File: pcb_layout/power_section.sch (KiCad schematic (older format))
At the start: 23 parts, among them Q1 NXP BSS84, U2 MCP73831/2, U3 TPS736

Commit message: More modules, initial pcb layout
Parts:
- C4: footprint Capacitors_SMD:C_0805 -> Capacitors_SMD:C_1206
- C5: value 4.7u -> 4.7uF; footprint Capacitors_SMD:C_0805 -> Capacitors_SMD:C_1206
- RF_Current1: footprint Socket_Strips:Socket_Strip_Angled_1x02_Pitch2.54mm -> Socket_Strips:Socket_Strip_Straight_1x02_Pitch2.54mm
- renumbered BATTERY1 to Battery_Input1, D2 to D1, D1 to Power_LED1
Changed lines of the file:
@@
 $EndDescr
 $Comp
-L GND #PWR19
+L GND #PWR09
 U 1 1 589A2DFC
 P 7850 2650
-F 0 "#PWR19" H 7850 2400 50  0001 C CNN
+F 0 "#PWR09" H 7850 2400 50  0001 C CNN
 F 1 "GND" H 7850 2500 50  0000 C CNN
 F 2 "" H 7850 2650 50  0000 C CNN
@@
 $EndComp
 $Comp
-L +3.3V #PWR16
+L +3.3V #PWR010
 U 1 1 589A2E1E
 P 6550 4050
-F 0 "#PWR16" H 6550 3900 50  0001 C CNN
+F 0 "#PWR010" H 6550 3900 50  0001 C CNN
 F 1 "+3.3V" H 6550 4190 50  0000 C CNN
 F 2 "" H 6550 4050 50  0000 C CNN
@@
 U 1 1 589A2E2B
 P 7200 3800
-F 0 "MCU_Current1" H 7200 3950 50  0000 C CNN
+F 0 "MCU_Current1" V 7400 3800 50  0000 C CNN
 F 1 "CONN_01X02" V 7300 3800 50  0000 C CNN
 F 2 "Socket_Strips:Socket_Strip_Straight_1x02_Pitch2.54mm" H 7200 3800 50  0001 C CNN
@@
 U 1 1 589A2E32
 P 7200 4650
-F 0 "RF_Current1" H 7200 4800 50  0000 C CNN
+F 0 "RF_Current1" V 7400 4650 50  0000 C CNN
 F 1 "CONN_01X02" V 7300 4650 50  0000 C CNN
-F 2 "Socket_Strips:Socket_Strip_Angled_1x02_Pitch2.54mm" H 7200 4650 50  0001 C CNN
+F 2 "Socket_Strips:Socket_Strip_Straight_1x02_Pitch2.54mm" H 7200 4650 50  0001 C CNN
 F 3 "" H 7200 4650 50  0000 C CNN
 	1    7200 4650
@@
 RF_POW
 $Comp
-L CONN_01X02 BATTERY1
+L CONN_01X02 Battery_Input1
 U 1 1 589A2E3B
 P 2700 2000
-F 0 "BATTERY1" H 2700 2300 50  0000 C CNN
+F 0 "Battery_Input1" H 2700 2300 50  0000 C CNN
 F 1 "CONN_01X02" V 2800 2000 50  0000 C CNN
 F 2 "Socket_Strips:Socket_Strip_Straight_1x02_Pitch2.54mm" H 2700 2000 50  0001 C CNN
@@
 $EndComp
 $Comp
-L GND #PWR10
+L GND #PWR011
 U 1 1 589A2E42
 P 2900 2700
-F 0 "#PWR10" H 2900 2450 50  0001 C CNN
+F 0 "#PWR011" H 2900 2450 50  0001 C CNN
 F 1 "GND" H 2900 2550 50  0000 C CNN
 F 2 "" H 2900 2700 50  0000 C CNN
@@
 $EndComp
 $Comp
-L GND #PWR12
+L GND #PWR012
 U 1 1 589A2E4F
 P 4000 2700
-F 0 "#PWR12" H 4000 2450 50  0001 C CNN
+F 0 "#PWR012" H 4000 2450 50  0001 C CNN
 F 1 "GND" H 4000 2550 50  0000 C CNN
 F 2 "" H 4000 2700 50  0000 C CNN
@@
 $EndComp
 $Comp
-L D_Zener D2
+L D_Zener D1
 U 1 1 589A2E55
 P 4400 2150
-F 0 "D2" H 4400 2250 50  0000 C CNN
+F 0 "D1" H 4400 2250 50  0000 C CNN
 F 1 "D_Zener" H 4400 2050 50  0000 C CNN
 F 2 "Diodes_SMD:D_SMA_Handsoldering" H 4400 2150 50  0001 C CNN
@@
 $EndComp
 $Comp
-L GND #PWR9
+L GND #PWR013
 U 1 1 589A2E64
 P 2450 4150
-F 0 "#PWR9" H 2450 3900 50  0001 C CNN
+F 0 "#PWR013" H 2450 3900 50  0001 C CNN
 F 1 "GND" H 2450 4000 50  0000 C CNN
 F 2 "" H 2450 4150 50  0000 C CNN
@@
 VUSB
 $Comp
-L LED D1
+L LED Power_LED1
 U 1 1 589A2E6D
 P 3550 3450
-F 0 "D1" H 3550 3550 50  0000 C CNN
+F 0 "Power_LED1" H 3550 3550 50  0000 C CNN
 F 1 "LED" H 3550 3350 50  0000 C CNN
 F 2 "LEDs:LED_0805" H 3550 3450 50  0001 C CNN
@@
 $EndComp
 $Comp
-L GND #PWR14
+L GND #PWR014
 U 1 1 589A2E83
 P 5050 4350
-F 0 "#PWR14" H 5050 4100 50  0001 C CNN
+F 0 "#PWR014" H 5050 4100 50  0001 C CNN
 F 1 "GND" H 5050 4200 50  0000 C CNN
 F 2 "" H 5050 4350 50  0000 C CNN
@@
 V_Battery
 $Comp
-L +3.3V #PWR17
+L +3.3V #PWR015
 U 1 1 589A2E91
 P 7400 2050
-F 0 "#PWR17" H 7400 1900 50  0001 C CNN
+F 0 "#PWR015" H 7400 1900 50  0001 C CNN
 F 1 "+3.3V" H 7400 2190 50  0000 C CNN
 F 2 "" H 7400 2050 50  0000 C CNN
@@
 $EndComp
 $Comp
-L GND #PWR15
+L GND #PWR016
 U 1 1 589A2E97
 P 5800 2350
-F 0 "#PWR15" H 5800 2100 50  0001 C CNN
+F 0 "#PWR016" H 5800 2100 50  0001 C CNN
 F 1 "GND" H 5800 2200 50  0000 C CNN
 F 2 "" H 5800 2350 50  0000 C CNN
@@
 $EndComp
 $Comp
-L GND #PWR18
+L GND #PWR017
 U 1 1 589A2EA4
 P 7400 2800
-F 0 "#PWR18" H 7400 2550 50  0001 C CNN
+F 0 "#PWR017" H 7400 2550 50  0001 C CNN
 F 1 "GND" H 7400 2650 50  0000 C CNN
 F 2 "" H 7400 2800 50  0000 C CNN
@@
 F 0 "C4" H 3475 2450 50  0000 L CNN
 F 1 "4.7uF" H 3475 2250 50  0000 L CNN
-F 2 "Capacitors_SMD:C_0805" H 3488 2200 50  0001 C CNN
+F 2 "Capacitors_SMD:C_1206" H 3488 2200 50  0001 C CNN
 F 3 "" H 3450 2350 50  0000 C CNN
 	1    3450 2350
@@
 $EndComp
 $Comp
-L GND #PWR11
+L GND #PWR018
 U 1 1 589A2EB1
 P 3450 2700
-F 0 "#PWR11" H 3450 2450 50  0001 C CNN
+F 0 "#PWR018" H 3450 2450 50  0001 C CNN
 F 1 "GND" H 3450 2550 50  0000 C CNN
 F 2 "" H 3450 2700 50  0000 C CNN
@@
 U 1 1 589A2EBE
 P 3550 4500
-F 0 "Charge_Current1" H 3550 4650 50  0000 C CNN
+F 0 "Charge_Current1" V 3750 4500 50  0000 C CNN
 F 1 "CONN_01X02" V 3650 4500 50  0000 C CNN
 F 2 "Socket_Strips:Socket_Strip_Straight_2x01_Pitch2.54mm" H 3550 4500 50  0001 C CNN
@@
 P 4750 4350
 F 0 "C5" H 4775 4450 50  0000 L CNN
-F 1 "4.7u" H 4775 4250 50  0000 L CNN
-F 2 "Capacitors_SMD:C_0805" H 4788 4200 50  0001 C CNN
+F 1 "4.7uF" H 4775 4250 50  0000 L CNN
+F 2 "Capacitors_SMD:C_1206" H 4788 4200 50  0001 C CNN
 F 3 "" H 4750 4350 50  0000 C CNN
 	1    4750 4350
@@
 $EndComp
 $Comp
-L GND #PWR13
+L GND #PWR019
 U 1 1 589A2ED3
 P 4750 4550
-F 0 "#PWR13" H 4750 4300 50  0001 C CNN
+F 0 "#PWR019" H 4750 4300 50  0001 C CNN
 F 1 "GND" H 4750 4400 50  0000 C CNN
 F 2 "" H 4750 4550 50  0000 C CNN
@@
 	8950 3100 9450 3100
 $Comp
-L GND #PWR20
+L GND #PWR020
 U 1 1 589A521E
 P 9050 3700
-F 0 "#PWR20" H 9050 3450 50  0001 C CNN
+F 0 "#PWR020" H 9050 3450 50  0001 C CNN
 F 1 "GND" H 9050 3550 50  0000 C CNN
 F 2 "" H 9050 3700 50  0000 C CNN
@@
 3.3V
 $Comp
-L +3.3V #PWR21
+L +3.3V #PWR021
 U 1 1 589A66AD
 P 9550 3100
-F 0 "#PWR21" H 9550 2950 50  0001 C CNN
+F 0 "#PWR021" H 9550 2950 50  0001 C CNN
 F 1 "+3.3V" H 9550 3240 50  0000 C CNN
 F 2 "" H 9550 3100 50  0000 C CNN

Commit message: Added PCB LAyout
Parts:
- Battery_Current1, Charge_Current1: footprint Socket_Strips:Socket_Strip_Straight_2x01_Pitch2.54mm -> Pin_Headers:Pin_Header_Straight_1x02_Pitch2.54mm
- Battery_Input1: footprint Socket_Strips:Socket_Strip_Straight_1x02_Pitch2.54mm -> Pin_Headers:Pin_Header_Angled_1x02_Pitch2.54mm
- MCU_Current1, RF_Current1: footprint Socket_Strips:Socket_Strip_Straight_1x02_Pitch2.54mm -> Pin_Headers:Pin_Header_Straight_1x02_Pitch2.54mm
- Power_LED1: symbol LED -> LED-RESCUE-lora_sensor
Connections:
- net labels removed: Gnd
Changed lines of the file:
@@
 LIBS:mcp9700t-e
 LIBS:rn2483
+LIBS:fa_238
 LIBS:lora_sensor-cache
-EELAYER 25 0
+EELAYER 26 0
 EELAYER END
 $Descr A4 11693 8268
@@
 F 0 "MCU_Current1" V 7400 3800 50  0000 C CNN
 F 1 "CONN_01X02" V 7300 3800 50  0000 C CNN
-F 2 "Socket_Strips:Socket_Strip_Straight_1x02_Pitch2.54mm" H 7200 3800 50  0001 C CNN
+F 2 "Pin_Headers:Pin_Header_Straight_1x02_Pitch2.54mm" H 7200 3800 50  0001 C CNN
 F 3 "" H 7200 3800 50  0000 C CNN
 	1    7200 3800
@@
 F 0 "RF_Current1" V 7400 4650 50  0000 C CNN
 F 1 "CONN_01X02" V 7300 4650 50  0000 C CNN
-F 2 "Socket_Strips:Socket_Strip_Straight_1x02_Pitch2.54mm" H 7200 4650 50  0001 C CNN
+F 2 "Pin_Headers:Pin_Header_Straight_1x02_Pitch2.54mm" H 7200 4650 50  0001 C CNN
 F 3 "" H 7200 4650 50  0000 C CNN
 	1    7200 4650
@@
 F 0 "Battery_Input1" H 2700 2300 50  0000 C CNN
 F 1 "CONN_01X02" V 2800 2000 50  0000 C CNN
-F 2 "Socket_Strips:Socket_Strip_Straight_1x02_Pitch2.54mm" H 2700 2000 50  0001 C CNN
+F 2 "Pin_Headers:Pin_Header_Angled_1x02_Pitch2.54mm" H 2700 2000 50  0001 C CNN
 F 3 "" H 2700 2000 50  0000 C CNN
 	1    2700 2000
@@
 VUSB
 $Comp
-L LED Power_LED1
+L LED-RESCUE-lora_sensor Power_LED1
 U 1 1 589A2E6D
 P 3550 3450
+AR Path="/589A2E6D" Ref="Power_LED1"  Part="1"
+AR Path="/5899E1BE/589A2E6D" Ref="Power_LED1"  Part="1"
 F 0 "Power_LED1" H 3550 3550 50  0000 C CNN
 F 1 "LED" H 3550 3350 50  0000 C CNN
@@
 F 0 "Battery_Current1" V 6300 1850 50  0000 C CNN
 F 1 "CONN_01X02" V 6250 1850 50  0000 C CNN
-F 2 "Socket_Strips:Socket_Strip_Straight_2x01_Pitch2.54mm" H 6150 1850 50  0001 C CNN
+F 2 "Pin_Headers:Pin_Header_Straight_1x02_Pitch2.54mm" H 6150 1850 50  0001 C CNN
 F 3 "" H 6150 1850 50  0000 C CNN
 	1    6150 1850
@@
 F 0 "Charge_Current1" V 3750 4500 50  0000 C CNN
 F 1 "CONN_01X02" V 3650 4500 50  0000 C CNN
-F 2 "Socket_Strips:Socket_Strip_Straight_2x01_Pitch2.54mm" H 3550 4500 50  0001 C CNN
+F 2 "Pin_Headers:Pin_Header_Straight_1x02_Pitch2.54mm" H 3550 4500 50  0001 C CNN
 F 3 "" H 3550 4500 50  0000 C CNN
 	1    3550 4500
@@
 	8950 3400 9450 3400
 Text HLabel 8950 3600 0    60   Input ~ 0
-Gnd
+GND
 Text HLabel 8950 3400 0    60   Input ~ 0
 RF_Power

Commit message: Finalized layout, added gerbers and renders
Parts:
- Battery_Input1: footprint Pin_Headers:Pin_Header_Angled_1x02_Pitch2.54mm -> Pin_Headers:Pin_Header_Straight_1x02_Pitch2.54mm
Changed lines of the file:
@@
 F 0 "Battery_Input1" H 2700 2300 50  0000 C CNN
 F 1 "CONN_01X02" V 2800 2000 50  0000 C CNN
-F 2 "Pin_Headers:Pin_Header_Angled_1x02_Pitch2.54mm" H 2700 2000 50  0001 C CNN
+F 2 "Pin_Headers:Pin_Header_Straight_1x02_Pitch2.54mm" H 2700 2000 50  0001 C CNN
 F 3 "" H 2700 2000 50  0000 C CNN
 	1    2700 2000

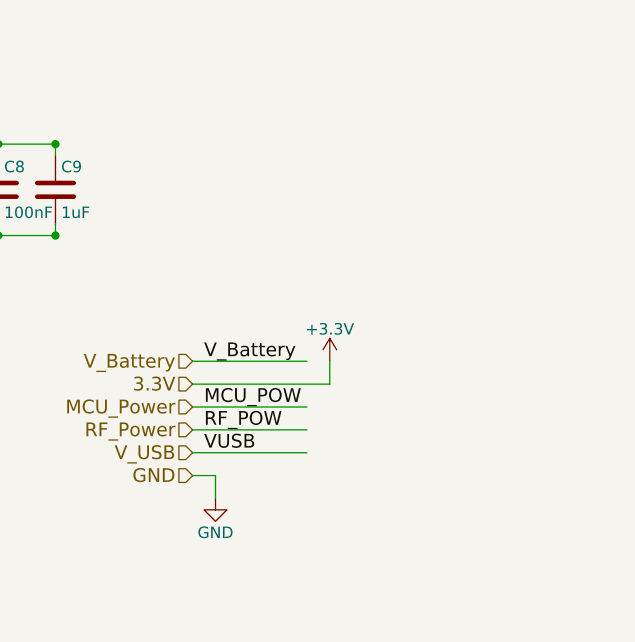
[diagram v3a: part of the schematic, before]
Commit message: More layout updates
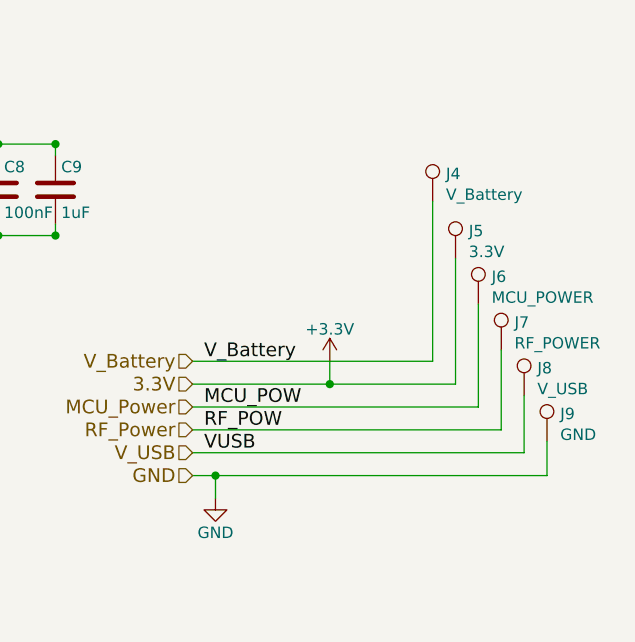
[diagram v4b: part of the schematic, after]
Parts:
- added J4: V_Battery, Measurement_Points:Measurement_Point_Square-SMD-Pad_Small, symbol TEST_1P
- added J5: 3.3V, Measurement_Points:Measurement_Point_Square-SMD-Pad_Small, symbol TEST_1P
- added J6: MCU_POWER, Measurement_Points:Measurement_Point_Square-SMD-Pad_Small, symbol TEST_1P
- added J7: RF_POWER, Measurement_Points:Measurement_Point_Square-SMD-Pad_Small, symbol TEST_1P
- added J8: V_USB, Measurement_Points:Measurement_Point_Square-SMD-Pad_Small, symbol TEST_1P
- added J9: GND, Measurement_Points:Measurement_Point_Square-TH_Big, symbol TEST_1P
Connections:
- wire segments 69 -> 75
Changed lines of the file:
@@
 V_Battery
 Wire Wire Line
-	8950 3100 9450 3100
+	8950 3100 10000 3100
 $Comp
 L GND #PWR020
@@
 V_Battery
 Wire Wire Line
-	8950 3600 9050 3600
+	8950 3600 10500 3600
 Wire Wire Line
 	9050 3600 9050 3700
 Wire Wire Line
-	8950 3200 9550 3200
+	8950 3200 10100 3200
 Text Label 9000 3300 0    60   ~ 0
 MCU_POW
@@
 RF_POW
 Wire Wire Line
-	8950 3300 9450 3300
+	8950 3300 10200 3300
 Wire Wire Line
-	8950 3400 9450 3400
+	8950 3400 10300 3400
 Text HLabel 8950 3600 0    60   Input ~ 0
 GND
@@
 VUSB
 Wire Wire Line
-	8950 3500 9450 3500
+	8950 3500 10400 3500
+$Comp
+L TEST_1P J4
+U 1 1 58A163E9
+P 10000 2400
+F 0 "J4" H 10058 2520 50  0000 L CNN
+F 1 "V_Battery" H 10058 2429 50  0000 L CNN
+F 2 "Measurement_Points:Measurement_Point_Square-SMD-Pad_Small" H 1850 950 50  0001 C CNN
+F 3 "" H 1850 950 50  0001 C CNN
+	1    10000 2400
+	1    0    0    -1
+$EndComp
+$Comp
+L TEST_1P J5
+U 1 1 58A16A2F
+P 10100 2650
+F 0 "J5" H 10158 2770 50  0000 L CNN
+F 1 "3.3V" H 10158 2679 50  0000 L CNN
+F 2 "Measurement_Points:Measurement_Point_Square-SMD-Pad_Small" H 1950 1200 50  0001 C CNN
+F 3 "" H 1950 1200 50  0001 C CNN
+	1    10100 2650
+	1    0    0    -1
+$EndComp
+$Comp
+L TEST_1P J6
+U 1 1 58A16A98
+P 10200 2850
+F 0 "J6" H 10258 2970 50  0000 L CNN
+F 1 "MCU_POWER" H 10258 2879 50  0000 L CNN
+F 2 "Measurement_Points:Measurement_Point_Square-SMD-Pad_Small" H 2050 1400 50  0001 C CNN
+F 3 "" H 2050 1400 50  0001 C CNN
+	1    10200 2850
+	1    0    0    -1
+$EndComp
+Wire Wire Line
+	10100 3200 10100 2650
+Connection ~ 9550 3200
+Wire Wire Line
+	10200 3300 10200 2850
+Wire Wire Line
+	10000 3100 10000 2400
+$Comp
+L TEST_1P J7
+U 1 1 58A16F1C
+P 10300 3050
+F 0 "J7" H 10358 3170 50  0000 L CNN
+F 1 "RF_POWER" H 10358 3079 50  0000 L CNN
+F 2 "Measurement_Points:Measurement_Point_Square-SMD-Pad_Small" H 2150 1600 50  0001 C CNN
+F 3 "" H 2150 1600 50  0001 C CNN
+	1    10300 3050
+	1    0    0    -1
+$EndComp
+Wire Wire Line
+	10300 3400 10300 3050
+$Comp
+L TEST_1P J8
+U 1 1 58A16FFC
+P 10400 3250
+F 0 "J8" H 10458 3370 50  0000 L CNN
+F 1 "V_USB" H 10458 3279 50  0000 L CNN
+F 2 "Measurement_Points:Measurement_Point_Square-SMD-Pad_Small" H 2250 1800 50  0001 C CNN
+F 3 "" H 2250 1800 50  0001 C CNN
+	1    10400 3250
+	1    0    0    -1
+$EndComp
+Wire Wire Line
+	10400 3500 10400 3250
+$Comp
+L TEST_1P J9
+U 1 1 58A170DB
+P 10500 3450
+F 0 "J9" H 10558 3570 50  0000 L CNN
+F 1 "GND" H 10558 3479 50  0000 L CNN
+F 2 "Measurement_Points:Measurement_Point_Square-TH_Big" H 2350 2000 50  0001 C CNN
+F 3 "" H 2350 2000 50  0001 C CNN
+	1    10500 3450
+	1    0    0    -1
+$EndComp
+Wire Wire Line
+	10500 3600 10500 3450
+Connection ~ 9050 3600
 $EndSCHEMATC

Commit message: Manufactured version
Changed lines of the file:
@@
 P 3550 3450
 AR Path="/589A2E6D" Ref="Power_LED1"  Part="1"
-AR Path="/5899E1BE/589A2E6D" Ref="Power_LED1"  Part="1"
-F 0 "Power_LED1" H 3550 3550 50  0000 C CNN
+AR Path="/5899E1BE/589A2E6D" Ref="Charge_LED1"  Part="1"
+F 0 "Charge_LED1" H 3550 3550 50  0000 C CNN
 F 1 "LED" H 3550 3350 50  0000 C CNN
 F 2 "LEDs:LED_0805" H 3550 3450 50  0001 C CNN
